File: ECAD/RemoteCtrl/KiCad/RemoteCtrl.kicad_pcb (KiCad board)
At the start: 2 copper layers, 101.6 x 81.3 mm, 83 parts, among them J1 UI, SW1 MX1A-E1NW, SW2 MX1A-E1NW, SW3 MX1A-E1NW, SW4 MX1A-E1NW, SW5 MX1A-E1NW, SW6 MX1A-E1NW, SW7 MX1A-E1NW, SW8 MX1A-E1NW, U1 74LVC1G17, U2 74LVC1G17, U3 74LVC1G17, U4 74LVC1G17, U5 74LVC1G17, U6 74LVC1G17, U7 74LVC1G17, U8 74LVC1G17

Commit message: Remote control work.
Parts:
- moved H2 11.6 mm to (191.1, 44.5)
- moved H1 11.4 mm to (97.2, 44.5)
- moved D1 11.4 mm to (108.0, 48.3)
- moved D10 11.4 mm to (160.0, 54.6)
- moved D11 11.4 mm to (160.0, 61.0)
- moved D2 11.4 mm to (108.0, 54.6)
- moved D7 11.4 mm to (134.6, 54.6)
- moved D8 11.4 mm to (134.6, 48.3)
- moved D9 11.4 mm to (160.0, 48.3)
- moved R1 11.4 mm to (104.1, 48.3)
- moved R10 11.4 mm to (156.2, 54.6)
- moved R11 11.4 mm to (156.2, 61.0)
- moved R2 11.4 mm to (104.1, 54.6)
- moved R7 11.4 mm to (130.8, 54.6)
- moved R8 11.4 mm to (130.8, 48.3)
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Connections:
- R8 pad 2: GND -> +5V
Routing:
- net +5V: track 248.5 -> 83.9 mm
- net /LED_Halted_Inst: track 109.2 -> 0.00 mm, vias 1 -> 0
- net /BTN_INC_CLK_F: track 124.6 -> 19.6 mm, vias 5 -> 0
- net /LED_Halted_Step: track 100.6 -> 0.00 mm, vias 1 -> 0
- net /BTN_DEC_CLK_F: track 108.3 -> 19.6 mm
- net /LED_Halted_Bkpt: track 88.0 -> 0.00 mm, vias 1 -> 0
- net /BTN_CLK_STEP_EN: track 82.8 -> 0.00 mm, vias 1 -> 0
- net /LED_CLK_STEP_EN: track 76.9 -> 0.00 mm, vias 5 -> 0
- net /LED_INT_Active: track 74.3 -> 0.00 mm, vias 4 -> 0
- net /BTN_CLK_STEP: track 90.2 -> 19.6 mm, vias 1 -> 0
- net /RESET: track 65.9 -> 0.00 mm, vias 3 -> 0
- net /BTN_INST_STEP_EN: track 62.5 -> 0.00 mm, vias 1 -> 0
- net /LED_INST_STEP_EN: track 61.0 -> 0.00 mm, vias 5 -> 0
- net /LED_Halted: track 74.6 -> 16.4 mm, vias 1 -> 0
- net /BTN_INST_STEP: track 76.9 -> 19.5 mm, vias 1 -> 0
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- added copper zone on F.Cu, net +5V
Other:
- board outline removed
- board text removed: "Clock Freq. +"
- board text removed: "Clock Freq. -"
- board text removed: "Clock Step Enable"
- board text removed: "Instruction Step Enable"
- board text removed: "Interrupt"
- board text removed: "Manual Clock"
- board text removed: "Next Instruction"
- board text removed: "RESET"

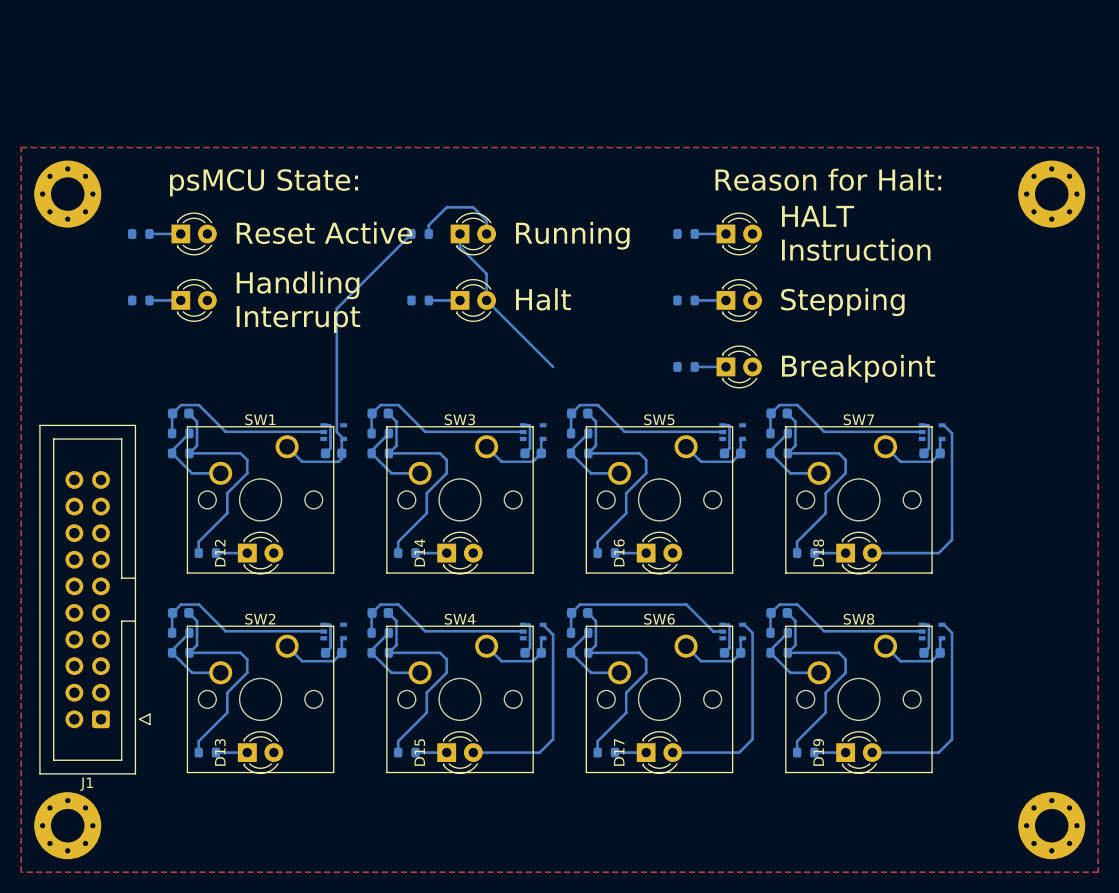
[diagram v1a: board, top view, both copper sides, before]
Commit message: Finished RemoteCtrl pcb
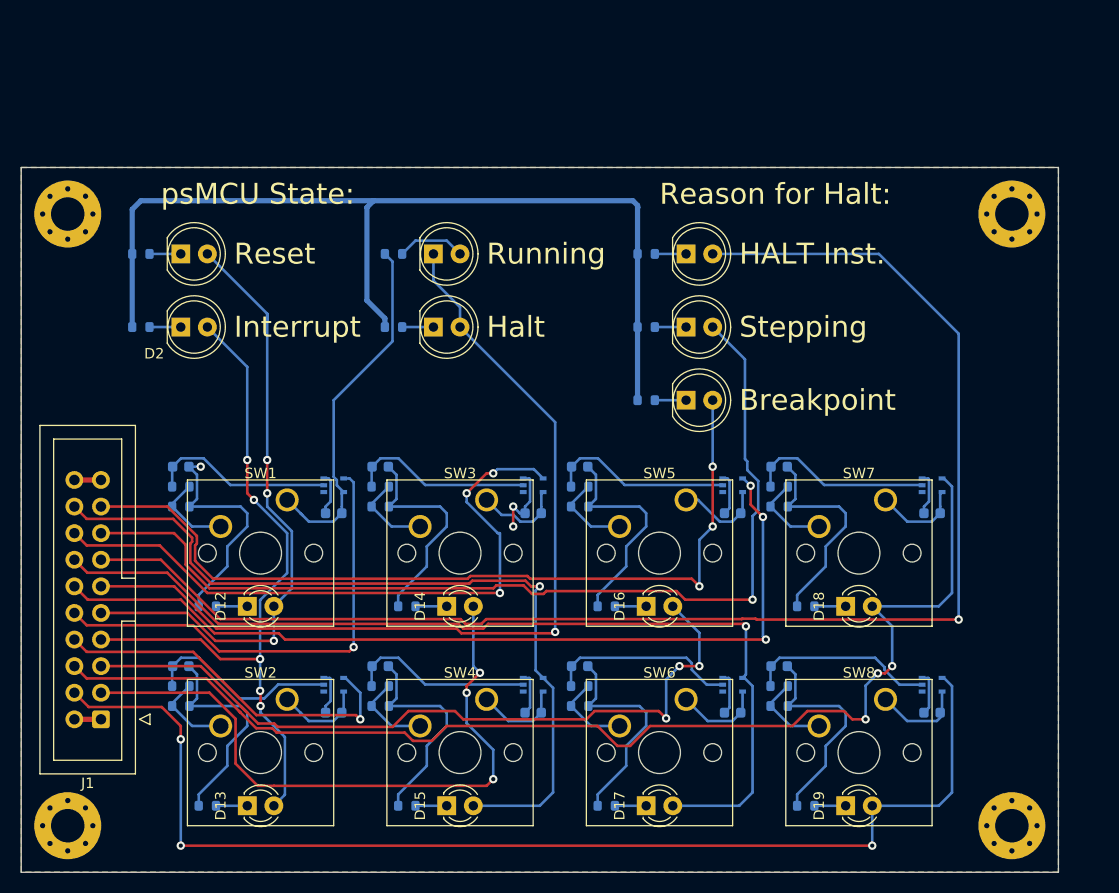
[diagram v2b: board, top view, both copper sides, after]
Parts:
- D1, D10, D11, D2, D7, D8, D9: footprint LED_THT:LED_D3.0mm -> LED_THT:LED_D5.0mm
- moved C10 5.72 mm to (160.7, 74.9)
- moved C12 5.72 mm to (160.7, 94.0)
- moved C14 5.72 mm to (179.7, 74.9)
- moved C16 5.72 mm to (179.7, 94.0)
- moved C2 5.72 mm to (122.6, 74.9)
- moved C4 5.72 mm to (122.6, 94.0)
- moved C6 5.72 mm to (141.6, 74.9)
- moved C8 5.72 mm to (141.6, 94.0)
- moved C1 5.08 mm to (108.0, 70.5)
- moved C11 5.08 mm to (146.1, 89.5)
- moved C13 5.08 mm to (165.1, 70.5)
- moved C15 5.08 mm to (165.1, 89.5)
- moved C3 5.08 mm to (108.0, 89.5)
- moved C5 5.08 mm to (127.0, 70.5)
- moved C7 5.08 mm to (127.0, 89.5)
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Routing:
- net /LED_Halted_Inst: track 0.00 -> 138.6 mm, vias 0 -> 1
- net GND: track 196.1 -> 318.2 mm, vias 0 -> 3
- net /BTN_INC_CLK_F: track 19.6 -> 114.4 mm, vias 0 -> 3
- net /LED_Halted_Step: track 0.00 -> 94.8 mm, vias 0 -> 1
- net /BTN_DEC_CLK_F: track 19.6 -> 112.3 mm, vias 0 -> 3
- net /BTN_CLK_STEP_EN: track 0.00 -> 84.5 mm, vias 0 -> 3
- net /LED_Halted_Bkpt: track 0.00 -> 80.5 mm, vias 0 -> 3
- net /LED_CLK_STEP_EN: track 0.00 -> 73.0 mm, vias 0 -> 3
- net /BTN_CLK_STEP: track 19.6 -> 91.8 mm, vias 0 -> 1
- net /LED_Halted: track 16.4 -> 86.2 mm, vias 0 -> 1
- net /LED_INT_Active: track 0.00 -> 67.6 mm, vias 0 -> 5
- net /BTN_INST_STEP_EN: track 0.00 -> 62.6 mm, vias 0 -> 3
- net /LED_INST_STEP_EN: track 0.00 -> 62.3 mm, vias 0 -> 3
- net /RESET: track 0.00 -> 59.3 mm, vias 0 -> 3
- net /BTN_INST_STEP: track 19.5 -> 78.2 mm, vias 0 -> 1
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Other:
- board outline added: 99.1 x 67.3 mm
- board text added: "HALT Inst."
- board text added: "Interrupt"
- board text added: "Reset"
- board text added: "v1.0"
- board text removed: "HALT Instruction"
- board text removed: "Handling Interrupt"
- board text removed: "Reset Active"
- board text removed: "v0.1"
